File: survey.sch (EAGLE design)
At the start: 20 parts

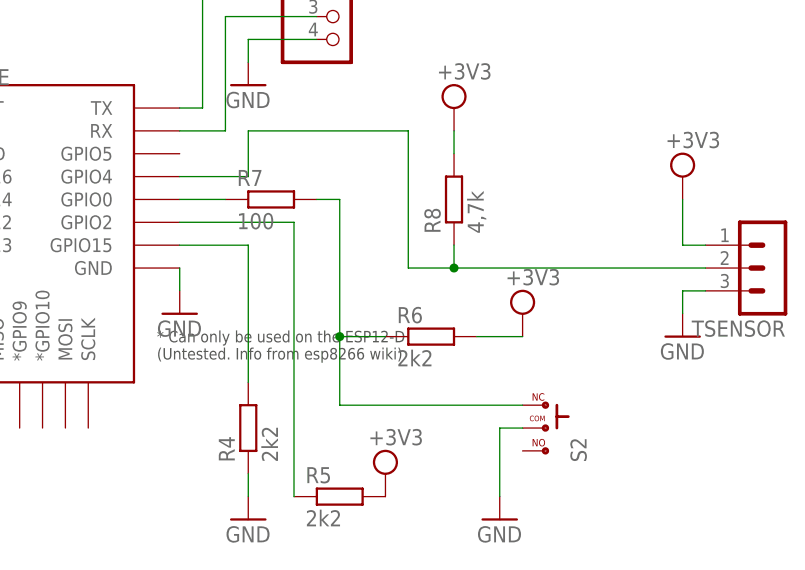
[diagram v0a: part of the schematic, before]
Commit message: Corrected programming switch connection.
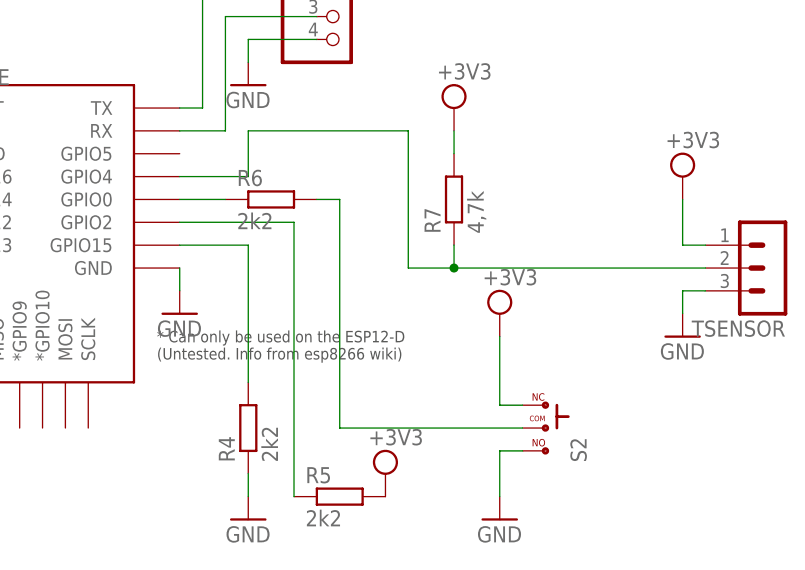
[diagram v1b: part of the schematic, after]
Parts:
- removed R8: 4,7k, rcl:R-EU_0204/7
- R7: value 100 -> 4,7k
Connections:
- net GND: now also S2.3; no longer S2.2
- net N$10: now also R6.1; no longer R7.1
- net N$5: now also R7.1; no longer R8.1
- net N$6: now also R6.2, S2.2; no longer R6.1, R7.2, S2.1
- net VCC: now also R7.2, S2.1; no longer R6.2, R8.2
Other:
- moved on the sheet: R6, R7
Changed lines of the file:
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@@
 <part name="GND8" library="supply1" library_urn="urn:adsk.eagle:library:371" deviceset="GND" device=""/>
 <part name="SUPPLY9" library="supply2" library_urn="urn:adsk.eagle:library:372" deviceset="VCC" device="" value="+3V3"/>
-<part name="R8" library="rcl" library_urn="urn:adsk.eagle:library:334" deviceset="R-EU_" device="0204/7" package3d_urn="urn:adsk.eagle:package:23498/1" value="4,7k"/>
+<part name="R7" library="rcl" library_urn="urn:adsk.eagle:library:334" deviceset="R-EU_" device="0204/7" package3d_urn="urn:adsk.eagle:package:23498/1" value="4,7k"/>
 <part name="S2" library="tango" deviceset="-SWITCH" device=""/>
 <part name="S1" library="switch-tact" deviceset="DTS-6" device=""/>
@@
 <part name="R6" library="rcl" library_urn="urn:adsk.eagle:library:334" deviceset="R-EU_" device="0204/7" package3d_urn="urn:adsk.eagle:package:23498/1" value="2k2"/>
 <part name="R2" library="rcl" library_urn="urn:adsk.eagle:library:334" deviceset="R-EU_" device="0204/7" package3d_urn="urn:adsk.eagle:package:23498/1" value="100"/>
-<part name="R7" library="rcl" library_urn="urn:adsk.eagle:library:334" deviceset="R-EU_" device="0204/7" package3d_urn="urn:adsk.eagle:package:23498/1" value="100"/>
 </parts>
 <sheets>
@@
 <instance part="GND3" gate="1" x="71.12" y="63.5"/>
 <instance part="GND6" gate="1" x="106.68" y="40.64"/>
-<instance part="SUPPLY6" gate="G$1" x="109.22" y="63.5"/>
+<instance part="SUPPLY6" gate="G$1" x="106.68" y="63.5"/>
 <instance part="SUPPLY7" gate="G$1" x="93.98" y="45.72"/>
 <instance part="SUPPLY8" gate="G$1" x="22.86" y="124.46"/>
@@
 <instance part="GND8" gate="1" x="78.74" y="40.64"/>
 <instance part="SUPPLY9" gate="G$1" x="101.6" y="86.36"/>
-<instance part="R8" gate="G$1" x="101.6" y="76.2" rot="R90"/>
+<instance part="R7" gate="G$1" x="101.6" y="76.2" rot="R90"/>
 <instance part="S2" gate="G$1" x="111.76" y="50.8"/>
 <instance part="S1" gate="G$1" x="15.24" y="104.14" rot="R270"/>
 <instance part="TSENSOR" gate="G$1" x="137.16" y="68.58" rot="R180"/>
 <instance part="R5" gate="G$1" x="88.9" y="43.18"/>
-<instance part="R6" gate="G$1" x="99.06" y="60.96"/>
+<instance part="R6" gate="G$1" x="81.28" y="76.2"/>
 <instance part="R2" gate="G$1" x="30.48" y="104.14"/>
-<instance part="R7" gate="G$1" x="81.28" y="76.2"/>
 </instances>
 <busses>
@@
 </segment>
 <segment>
-<wire x1="104.14" y1="60.96" x2="109.22" y2="60.96" width="0.1524" layer="91"/>
-<pinref part="SUPPLY6" gate="G$1" pin="VCC"/>
-<pinref part="R6" gate="G$1" pin="2"/>
-</segment>
-<segment>
 <pinref part="R1" gate="G$1" pin="2"/>
 <wire x1="22.86" y1="119.38" x2="22.86" y2="121.92" width="0.1524" layer="91"/>
@@
 </segment>
 <segment>
-<pinref part="R8" gate="G$1" pin="2"/>
+<pinref part="R7" gate="G$1" pin="2"/>
 <pinref part="SUPPLY9" gate="G$1" pin="VCC"/>
 <wire x1="101.6" y1="83.82" x2="101.6" y2="81.28" width="0.1524" layer="91"/>
@@
 <pinref part="SUPPLY7" gate="G$1" pin="VCC"/>
 <pinref part="R5" gate="G$1" pin="2"/>
+</segment>
+<segment>
+<pinref part="SUPPLY6" gate="G$1" pin="VCC"/>
+<wire x1="106.68" y1="60.96" x2="106.68" y2="53.34" width="0.1524" layer="91"/>
+<pinref part="S2" gate="G$1" pin="1"/>
+<wire x1="106.68" y1="53.34" x2="109.22" y2="53.34" width="0.1524" layer="91"/>
 </segment>
 </net>
@@
 </segment>
 <segment>
-<pinref part="S2" gate="G$1" pin="2"/>
-<wire x1="106.68" y1="43.18" x2="106.68" y2="50.8" width="0.1524" layer="91"/>
-<wire x1="106.68" y1="50.8" x2="109.22" y2="50.8" width="0.1524" layer="91"/>
-<pinref part="GND6" gate="1" pin="GND"/>
-</segment>
-<segment>
 <pinref part="TSENSOR" gate="G$1" pin="3"/>
 <wire x1="129.54" y1="66.04" x2="127" y2="66.04" width="0.1524" layer="91"/>
@@
 <pinref part="GND3" gate="1" pin="GND"/>
 <wire x1="71.12" y1="68.58" x2="71.12" y2="66.04" width="0.1524" layer="91"/>
+</segment>
+<segment>
+<pinref part="S2" gate="G$1" pin="3"/>
+<wire x1="109.22" y1="48.26" x2="106.68" y2="48.26" width="0.1524" layer="91"/>
+<pinref part="GND6" gate="1" pin="GND"/>
+<wire x1="106.68" y1="48.26" x2="106.68" y2="43.18" width="0.1524" layer="91"/>
 </segment>
 </net>
@@
 <wire x1="78.74" y1="83.82" x2="78.74" y2="78.74" width="0.1524" layer="91"/>
 <wire x1="96.52" y1="68.58" x2="101.6" y2="68.58" width="0.1524" layer="91"/>
-<pinref part="R8" gate="G$1" pin="1"/>
+<pinref part="R7" gate="G$1" pin="1"/>
 <wire x1="101.6" y1="68.58" x2="129.54" y2="68.58" width="0.1524" layer="91"/>
 <wire x1="101.6" y1="71.12" x2="101.6" y2="68.58" width="0.1524" layer="91"/>
@@
 <net name="N$6" class="0">
 <segment>
-<wire x1="88.9" y1="76.2" x2="88.9" y2="60.96" width="0.1524" layer="91"/>
-<wire x1="88.9" y1="60.96" x2="93.98" y2="60.96" width="0.1524" layer="91"/>
-<junction x="88.9" y="60.96"/>
-<wire x1="88.9" y1="60.96" x2="88.9" y2="53.34" width="0.1524" layer="91"/>
-<pinref part="S2" gate="G$1" pin="1"/>
-<wire x1="109.22" y1="53.34" x2="88.9" y2="53.34" width="0.1524" layer="91"/>
-<pinref part="R6" gate="G$1" pin="1"/>
-<pinref part="R7" gate="G$1" pin="2"/>
+<wire x1="88.9" y1="76.2" x2="88.9" y2="50.8" width="0.1524" layer="91"/>
 <wire x1="86.36" y1="76.2" x2="88.9" y2="76.2" width="0.1524" layer="91"/>
+<pinref part="R6" gate="G$1" pin="2"/>
+<pinref part="S2" gate="G$1" pin="2"/>
+<wire x1="88.9" y1="50.8" x2="109.22" y2="50.8" width="0.1524" layer="91"/>
 </segment>
 </net>
@@
 <net name="N$10" class="0">
 <segment>
-<pinref part="R7" gate="G$1" pin="1"/>
 <pinref part="ESP-12E" gate="G$1" pin="GPIO0"/>
 <wire x1="76.2" y1="76.2" x2="71.12" y2="76.2" width="0.1524" layer="91"/>
-</segment>
-</net>
+<pinref part="R6" gate="G$1" pin="1"/>
+</segment>
+</net>
